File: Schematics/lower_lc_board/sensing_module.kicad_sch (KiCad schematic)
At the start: 25 parts, among them J4 HALL-1, J5 HALL-2, Q3 2N7002, U11 DMP4065S-7, U9 ADC_ADS131M04IPWR

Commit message: PCB for review
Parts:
- added C2: 0.1uF, Capacitor_SMD:C_0603_1608Metric, symbol Device:C
- added FB1: FerriteBead, Resistor_SMD:R_0805_2012Metric, symbol Device:FerriteBead
- C26, C27, C56: LCSC C76599 -> C57112
- C29: LCSC C5378 -> C21120
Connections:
- net GND: now also C2.2
- net VPT: now also C2.1, FB1.1; no longer C35.1, U11.3 (D)
- new net: C35.1, FB1.2, U11.3 (D)
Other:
- note removed: "added to avoid constant power drain"
- moved on the sheet: C35

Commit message: WIP - i2c-2 refactor
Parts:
- C2: JLCPCB C14663 -> (none)
- C23: footprint Capacitor_SMD:C_0805_2012Metric -> Capacitor_SMD:C_0603_1608Metric; JLCPCB C49678 -> (none); LCSC (none) -> C49678
- C26, C27, C56: JLCPCB C57112 -> (none)
- C28, C43: JLCPCB C15849 -> (none)
- C29: JLCPCB C21120 -> (none)
- C33: footprint Capacitor_SMD:C_0805_2012Metric -> Capacitor_SMD:C_0603_1608Metric; JLCPCB C49678 -> (none); LCSC (none) -> C14663
- C35: JLCPCB C13585 -> (none); LCSC (none) -> C13585
- FB1: JLCPCB 1015 -> (none)
- Q3: JLCPCB C8545 -> (none)
- R17, R18: JLCPCB C4190 -> (none)
- R19, R20: JLCPCB C22765 -> (none)
- R22, R43, R49: JLCPCB C25804 -> (none); LCSC (none) -> C25804
- R23: value 4.7k -> 6.2k; footprint Resistor_SMD:R_0805_2012Metric -> Resistor_SMD:R_0603_1608Metric; JLCPCB C23162 -> (none); LCSC (none) -> C4260
- R25: JLCPCB C25804 -> (none)
- R44: JLCPCB C8218 -> (none); LCSC (none) -> C8218
- U11: JLCPCB C182476 -> (none)
- U9: JLCPCB C2862562 -> (none)
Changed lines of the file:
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@@
 			)
 		)
-		(property "JLCPCB" "C15849"
-			(at 182.88 40.64 0)
-			(effects
-				(font
-					(size 1.27 1.27)
-				)
-				(hide yes)
-			)
-		)
 		(property "Sim.Device" ""
 			(at 182.88 40.64 0)
@@
 			)
 		)
-		(property "JLCPCB" "C8545"
-			(at 223.52 59.69 0)
-			(effects
-				(font
-					(size 1.27 1.27)
-				)
-				(hide yes)
-			)
-		)
 		(property "Sim.Device" ""
 			(at 223.52 59.69 0)
@@
 			)
 		)
-		(property "JLCPCB" "C57112"
-			(at 135.89 71.12 0)
-			(effects
-				(font
-					(size 1.27 1.27)
-				)
-				(hide yes)
-			)
-		)
 		(property "Sim.Device" ""
 			(at 135.89 71.12 0)
@@
 			)
 		)
-		(property "Value" "4.7k"
+		(property "Value" "6.2k"
 			(at 230.378 73.66 90)
 			(effects
@@
 			)
 		)
-		(property "Footprint" "Resistor_SMD:R_0805_2012Metric"
+		(property "Footprint" "Resistor_SMD:R_0603_1608Metric"
 			(at 228.6 75.438 90)
 			(effects
@@
 			)
 		)
-		(property "JLCPCB" "C23162"
+		(property "Sim.Device" ""
 			(at 228.6 73.66 0)
 			(effects
@@
 			)
 		)
-		(property "Sim.Device" ""
+		(property "Sim.Pins" ""
 			(at 228.6 73.66 0)
 			(effects
@@
 			)
 		)
-		(property "Sim.Pins" ""
+		(property "LCSC" "C4260"
 			(at 228.6 73.66 0)
 			(effects
@@
 			)
 		)
-		(property "Footprint" "Capacitor_SMD:C_0805_2012Metric"
+		(property "Footprint" "Capacitor_SMD:C_0603_1608Metric"
 			(at 46.6852 173.99 0)
 			(effects
@@
 			)
 		)
-		(property "JLCPCB" "C49678"
+		(property "Sim.Device" ""
 			(at 45.72 170.18 0)
 			(effects
@@
 			)
 		)
-		(property "Sim.Device" ""
+		(property "Sim.Pins" ""
 			(at 45.72 170.18 0)
 			(effects
@@
 			)
 		)
-		(property "Sim.Pins" ""
+		(property "LCSC" "C14663"
 			(at 45.72 170.18 0)
 			(effects
@@
 			)
 		)
-		(property "JLCPCB" "C8218"
+		(property "Sim.Device" ""
 			(at 241.3 64.77 0)
 			(effects
@@
 			)
 		)
-		(property "Sim.Device" ""
+		(property "Sim.Pins" ""
 			(at 241.3 64.77 0)
 			(effects
@@
 			)
 		)
-		(property "Sim.Pins" ""
+		(property "LCSC" "C8218"
 			(at 241.3 64.77 0)
 			(effects
@@
 			)
 		)
-		(property "Footprint" "Capacitor_SMD:C_0805_2012Metric"
+		(property "Footprint" "Capacitor_SMD:C_0603_1608Metric"
 			(at 46.6852 134.62 0)
 			(effects
@@
 			)
 		)
-		(property "JLCPCB" "C49678"
+		(property "Sim.Device" ""
 			(at 45.72 130.81 0)
 			(effects
@@
 			)
 		)
-		(property "Sim.Device" ""
+		(property "Sim.Pins" ""
 			(at 45.72 130.81 0)
 			(effects
@@
 			)
 		)
-		(property "Sim.Pins" ""
+		(property "LCSC" "C49678"
 			(at 45.72 130.81 0)
 			(effects
@@
 			)
 		)
-		(property "JLCPCB" "1015"
-			(at 257.81 100.33 0)
-			(effects
-				(font
-					(size 1.27 1.27)
-				)
-				(hide yes)
-			)
-		)
 		(property "LCSC" "1015"
 			(at 257.81 100.33 0)
@@
 			)
 		)
-		(property "JLCPCB" "C14663"
-			(at 254 104.14 0)
-			(effects
-				(font
-					(size 1.27 1.27)
-				)
-				(hide yes)
-			)
-		)
 		(property "Sim.Device" ""
 			(at 254 104.14 0)
@@
 			)
 		)
-		(property "JLCPCB" "C22765"
-			(at 127 43.18 0)
-			(effects
-				(font
-					(size 1.27 1.27)
-				)
-				(hide yes)
-			)
-		)
 		(property "Sim.Device" ""
 			(at 127 43.18 0)
@@
 			)
 		)
-		(property "JLCPCB" "C57112"
-			(at 134.62 60.96 0)
-			(effects
-				(font
-					(size 1.27 1.27)
-				)
-				(hide yes)
-			)
-		)
 		(property "Sim.Device" ""
 			(at 134.62 60.96 0)
@@
 			)
 		)
-		(property "JLCPCB" "C4190"
-			(at 91.44 128.27 0)
-			(effects
-				(font
-					(size 1.27 1.27)
-				)
-				(hide yes)
-			)
-		)
 		(property "Sim.Device" ""
 			(at 91.44 128.27 0)
@@
 			)
 		)
-		(property "JLCPCB" "C15849"
-			(at 200.66 43.18 0)
-			(effects
-				(font
-					(size 1.27 1.27)
-				)
-				(hide yes)
-			)
-		)
 		(property "Sim.Device" ""
 			(at 200.66 43.18 0)
@@
 			)
 		)
-		(property "JLCPCB" "C22765"
-			(at 128.27 57.15 0)
-			(effects
-				(font
-					(size 1.27 1.27)
-				)
-				(hide yes)
-			)
-		)
 		(property "Sim.Device" ""
 			(at 128.27 57.15 0)
@@
 			)
 		)
-		(property "JLCPCB" "C25804"
-			(at 118.11 177.8 0)
-			(effects
-				(font
-					(size 1.27 1.27)
-				)
-				(hide yes)
-			)
-		)
 		(property "Sim.Device" ""
 			(at 118.11 177.8 0)
@@
 			)
 		)
-		(property "JLCPCB" "C21120"
-			(at 186.69 74.93 0)
-			(effects
-				(font
-					(size 1.27 1.27)
-				)
-				(hide yes)
-			)
-		)
 		(property "Sim.Device" ""
 			(at 186.69 74.93 0)
@@
 			)
 		)
-		(property "JLCPCB" "C57112"
-			(at 133.35 46.99 0)
-			(effects
-				(font
-					(size 1.27 1.27)
-				)
-				(hide yes)
-			)
-		)
 		(property "Sim.Device" ""
 			(at 133.35 46.99 0)
@@
 			)
 		)
-		(property "JLCPCB" "C182476"
-			(at 229.87 80.01 0)
-			(effects
-				(font
-					(size 1.27 1.27)
-				)
-				(hide yes)
-			)
-		)
 		(property "LCSC" "C182476"
 			(at 229.87 80.01 0)
@@
 			)
 		)
-		(property "JLCPCB" "C25804"
+		(property "Sim.Device" ""
 			(at 203.2 82.55 0)
 			(effects
@@
 			)
 		)
-		(property "Sim.Device" ""
+		(property "Sim.Pins" ""
 			(at 203.2 82.55 0)
 			(effects
@@
 			)
 		)
-		(property "Sim.Pins" ""
+		(property "LCSC" "C25804"
 			(at 203.2 82.55 0)
 			(effects
@@
 			)
 		)
-		(property "JLCPCB" "C25804"
+		(property "Sim.Device" ""
 			(at 234.95 68.58 0)
 			(effects
@@
 			)
 		)
-		(property "Sim.Device" ""
+		(property "Sim.Pins" ""
 			(at 234.95 68.58 0)
 			(effects
@@
 			)
 		)
-		(property "Sim.Pins" ""
+		(property "LCSC" "C25804"
 			(at 234.95 68.58 0)
 			(effects
@@
 			)
 		)
-		(property "JLCPCB" "C4190"
-			(at 91.44 144.78 0)
-			(effects
-				(font
-					(size 1.27 1.27)
-				)
-				(hide yes)
-			)
-		)
 		(property "Sim.Device" ""
 			(at 91.44 144.78 0)
@@
 			)
 		)
-		(property "JLCPCB" "C25804"
+		(property "Sim.Device" ""
 			(at 218.44 73.66 0)
 			(effects
@@
 			)
 		)
-		(property "Sim.Device" ""
+		(property "Sim.Pins" ""
 			(at 218.44 73.66 0)
 			(effects
@@
 			)
 		)
-		(property "Sim.Pins" ""
+		(property "LCSC" "C25804"
 			(at 218.44 73.66 0)
 			(effects
@@
 			)
 		)
-		(property "JLCPCB" "C13585"
+		(property "Sim.Device" ""
 			(at 261.62 104.14 0)
 			(effects
@@
 			)
 		)
-		(property "Sim.Device" ""
+		(property "Sim.Pins" ""
 			(at 261.62 104.14 0)
 			(effects
@@
 			)
 		)
-		(property "Sim.Pins" ""
+		(property "LCSC" "C13585"
 			(at 261.62 104.14 0)
 			(effects
@@
 			(at 162.56 64.77 0)
 			(effects
-				(font
-					(size 1.27 1.27)
-				)
-				(hide yes)
-			)
-		)
-		(property "JLCPCB" "C2862562"
-			(at 162.56 64.77 0)
-			(effects

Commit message: start 2nd refactor
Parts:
- added R21, R45: 2.2k, Resistor_SMD:R_0402_1005Metric, symbol Device:R
- R17, R18: footprint Resistor_SMD:R_0603_1608Metric -> Resistor_SMD:R_0402_1005Metric; LCSC C4190 -> C25879
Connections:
- net +3V3: now also R21.2, R45.1
- net HALL_SCL renamed HALL_SCL1
- net HALL_SCL1: no longer J5.3 (Pin_3)
- net HALL_SDA renamed HALL_SDA1
- net HALL_SDA1: no longer J5.2 (Pin_2)
- new net HALL_SCL2: J5.3 (Pin_3), R45.2
- new net HALL_SDA2: J5.2 (Pin_2), R21.1
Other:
- moved on the sheet: R17, R18

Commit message: updates and added to cart
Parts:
- added C18: 0.1uF, Capacitor_SMD:C_0603_1608Metric, symbol Device:C
- C23: LCSC C49678 -> C14663
- FB1: value FerriteBead -> 600R; footprint Resistor_SMD:R_0805_2012Metric -> Resistor_SMD:R_0603_1608Metric; LCSC 1015 -> C1002
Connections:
- net +3V3: now also R49.2; no longer R49.1
- net ADC_CS: now also R49.1; no longer R49.2
- net GND: now also C18.2
- net VPT: now also C18.1
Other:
- sheet PT-1 ports: added none; removed IN
- note removed: "* as of 03-25-2026 - removed TC2 - replaced JST conns with molex Nano series"
- note removed: "Incase of Voltage Spike"
- note removed: "Vf = 1.25v (at 100ma), Vmax = 3.3+1.25, 0.95v/5ma ~ 200ohms current limiter"
- note removed: "assuming LVCMOS output impedance of 25ohms so 33+25=58ohms"
- title: HYDRA | Sensing Circuitry -> Sensing Circuitry
- moved on the sheet: C29, R25, TH1

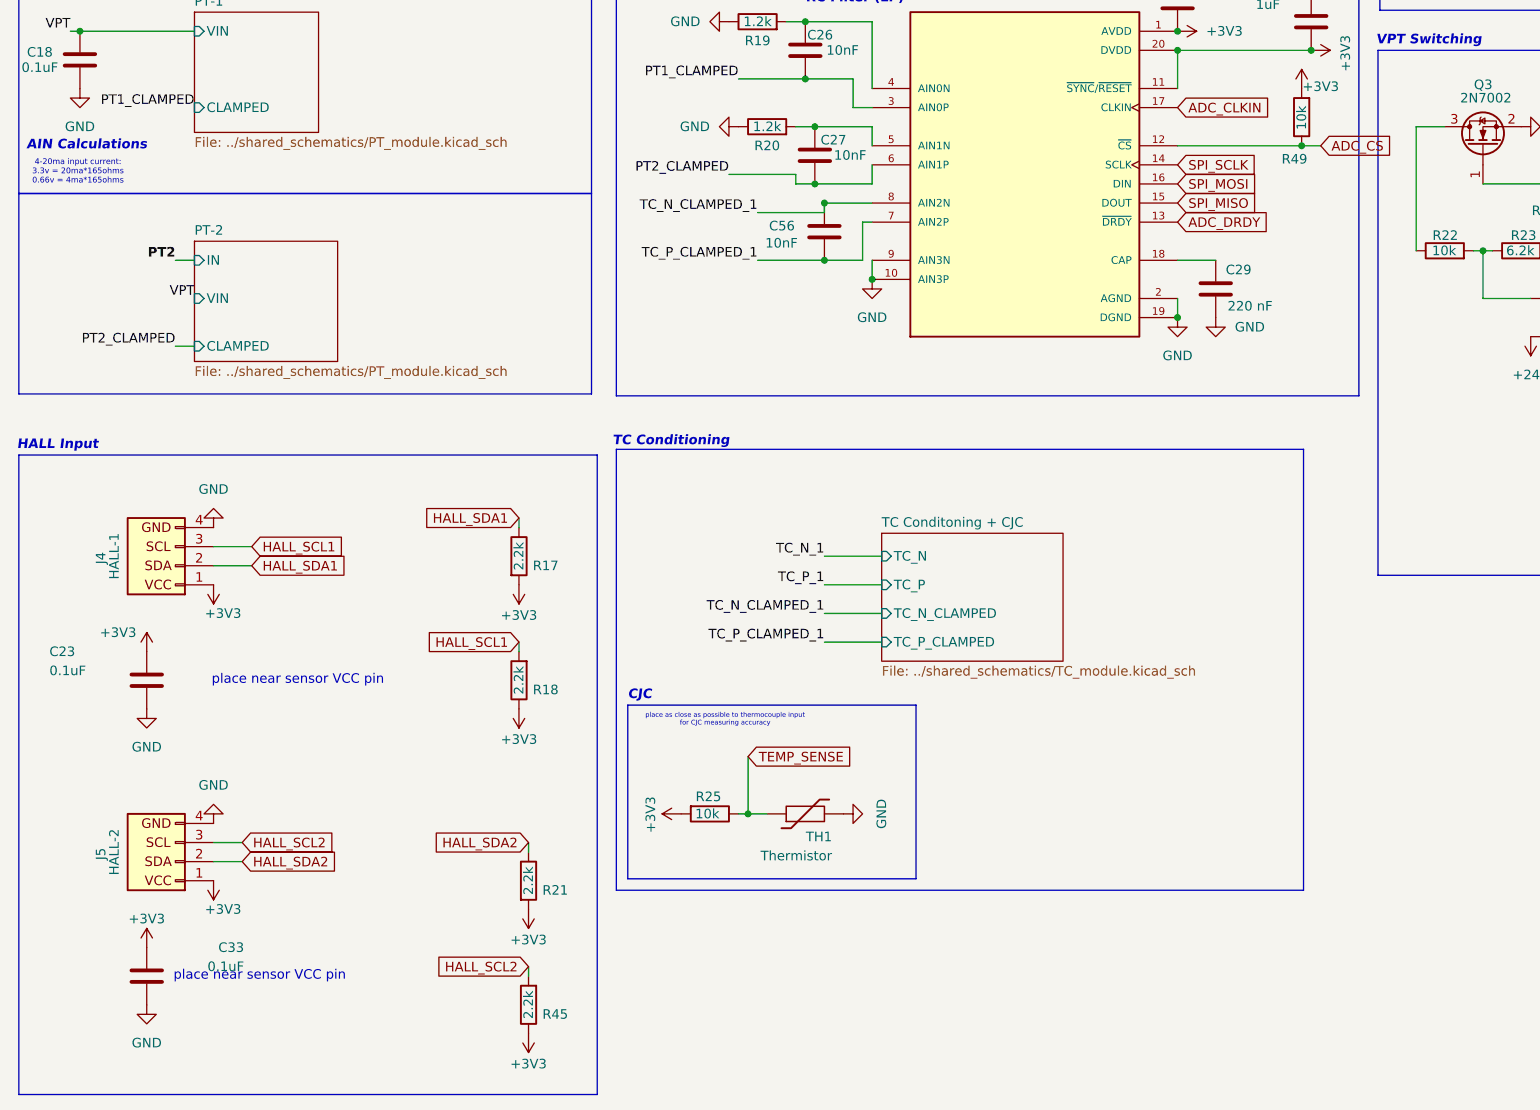
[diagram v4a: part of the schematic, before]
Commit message: add board-specifc READMEs (TODO), cleanup schematic titles
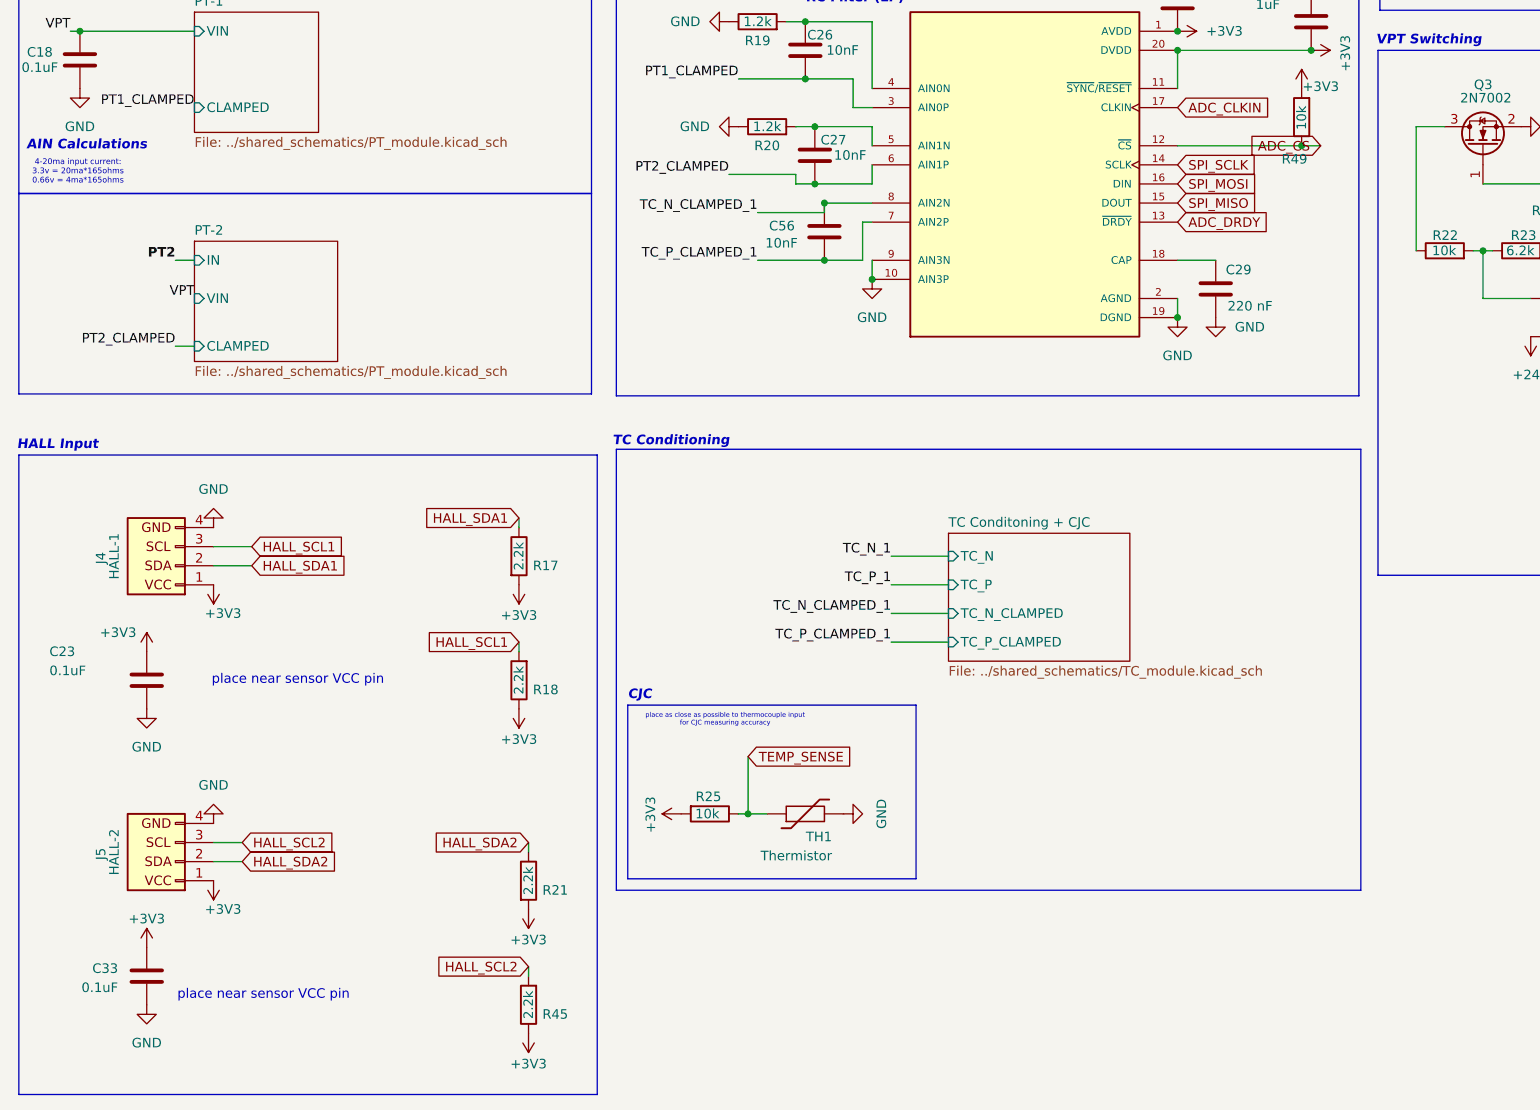
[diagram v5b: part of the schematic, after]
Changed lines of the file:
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@@
 		(title "Sensing Circuitry")
 		(company "Queen's Rocket Engineering Team")
-		(comment 1 "Jeevan Sanchez")
+		(comment 1 "Contributors: Jeevan Sanchez, Tristan Alderson")
+		(comment 2 "HYDRA - Lower Control Board")
 	)
 	(junction
@@
 	(wire
 		(pts
-			(xy 135.89 114.3) (xy 143.51 114.3)
+			(xy 144.78 114.3) (xy 152.4 114.3)
 		)
 		(stroke
@@
 	(wire
 		(pts
-			(xy 135.89 118.11) (xy 143.51 118.11)
+			(xy 144.78 118.11) (xy 152.4 118.11)
 		)
 		(stroke
@@
 	(wire
 		(pts
-			(xy 135.89 125.73) (xy 143.51 125.73)
+			(xy 144.78 125.73) (xy 152.4 125.73)
 		)
 		(stroke
@@
 	(wire
 		(pts
-			(xy 135.89 121.92) (xy 143.51 121.92)
+			(xy 144.78 121.92) (xy 152.4 121.92)
 		)
 		(stroke
@@
 	(rectangle
 		(start 108.204 100.076)
-		(end 199.644 158.75)
+		(end 207.264 158.75)
 		(stroke
 			(width 0)
@@
 	(text "place near sensor VCC pin"
 		(exclude_from_sim no)
-		(at 49.276 170.18 0)
+		(at 49.784 172.72 0)
 		(effects
 			(font
@@
 	)
 	(label "TC_P_1"
-		(at 135.89 118.11 180)
+		(at 144.78 118.11 180)
 		(fields_autoplaced yes)
 		(effects
@@
 	)
 	(label "TC_N_CLAMPED_1"
-		(at 135.89 121.92 180)
+		(at 144.78 121.92 180)
 		(fields_autoplaced yes)
 		(effects
@@
 	)
 	(label "TC_N_1"
-		(at 135.89 114.3 180)
+		(at 144.78 114.3 180)
 		(fields_autoplaced yes)
 		(effects
@@
 	)
 	(label "TC_P_CLAMPED_1"
-		(at 135.89 125.73 180)
+		(at 144.78 125.73 180)
 		(fields_autoplaced yes)
 		(effects
@@
 	(global_label "ADC_CS"
 		(shape input)
-		(at 201.93 59.69 0)
+		(at 201.93 59.69 180)
 		(fields_autoplaced yes)
 		(effects
@@
 				(size 1.27 1.27)
 			)
-			(justify left)
+			(justify right)
 		)
 		(property "Intersheetrefs" "${INTERSHEET_REFS}"
-			(at 211.9909 59.69 0)
+			(at 191.8691 59.69 0)
 			(effects
 				(font
 					(size 1.27 1.27)
 				)
-				(justify left)
+				(justify right)
 				(hide yes)
 			)
@@
 		(dnp no)
 		(property "Reference" "C33"
-			(at 58.674 166.37 0)
+			(at 41.91 169.164 0)
 			(effects
 				(font
@@
 		)
 		(property "Value" "0.1uF"
-			(at 58.674 168.91 0)
+			(at 41.91 171.704 0)
 			(effects
 				(font
@@
 	)
 	(sheet
-		(at 143.51 111.252)
+		(at 152.4 111.252)
 		(size 24.13 17.018)
 		(fields_autoplaced yes)
@@
 		)
 		(property "Sheetname" "TC Conditoning + CJC"
-			(at 143.51 110.5404 0)
+			(at 152.4 110.5404 0)
 			(effects
 				(font
@@
 		)
 		(property "Sheetfile" "../shared_schematics/TC_module.kicad_sch"
-			(at 143.51 128.8546 0)
+			(at 152.4 128.8546 0)
 			(effects
 				(font
@@
 		)
 		(pin "TC_N_CLAMPED" input
-			(at 143.51 121.92 180)
+			(at 152.4 121.92 180)
 			(effects
 				(font
@@
 		)
 		(pin "TC_N" input
-			(at 143.51 114.3 180)
+			(at 152.4 114.3 180)
 			(effects
 				(font
@@
 		)
 		(pin "TC_P" input
-			(at 143.51 118.11 180)
+			(at 152.4 118.11 180)
 			(effects
 				(font
@@
 		)
 		(pin "TC_P_CLAMPED" input
-			(at 143.51 125.73 180)
+			(at 152.4 125.73 180)
 			(effects
 				(font

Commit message: add ed pinouts
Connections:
- net TEMP_SENSE renamed CJC_SENSE
- net VPT-SW renamed VPT_EN
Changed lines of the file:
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@@
 		)
 	)
-	(global_label "VPT-SW"
+	(global_label "VPT_EN"
 		(shape input)
 		(at 245.11 64.77 0)
@@
 		)
 		(property "Intersheetrefs" "${INTERSHEET_REFS}"
-			(at 255.6547 64.77 0)
+			(at 254.8685 64.77 0)
 			(effects
 				(font
@@
 		)
 	)
-	(global_label "TEMP_SENSE"
+	(global_label "CJC_SENSE"
 		(shape input)
 		(at 125.73 140.97 0)
@@
 		)
 		(property "Intersheetrefs" "${INTERSHEET_REFS}"
-			(at 140.5683 140.97 0)
+			(at 139.2379 140.97 0)
 			(effects
 				(font
